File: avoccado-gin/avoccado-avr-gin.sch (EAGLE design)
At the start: 61 parts, among them Q1 16MHz, Q2 FET, U1 MPU-6000QFN-24, U2 MCP73831

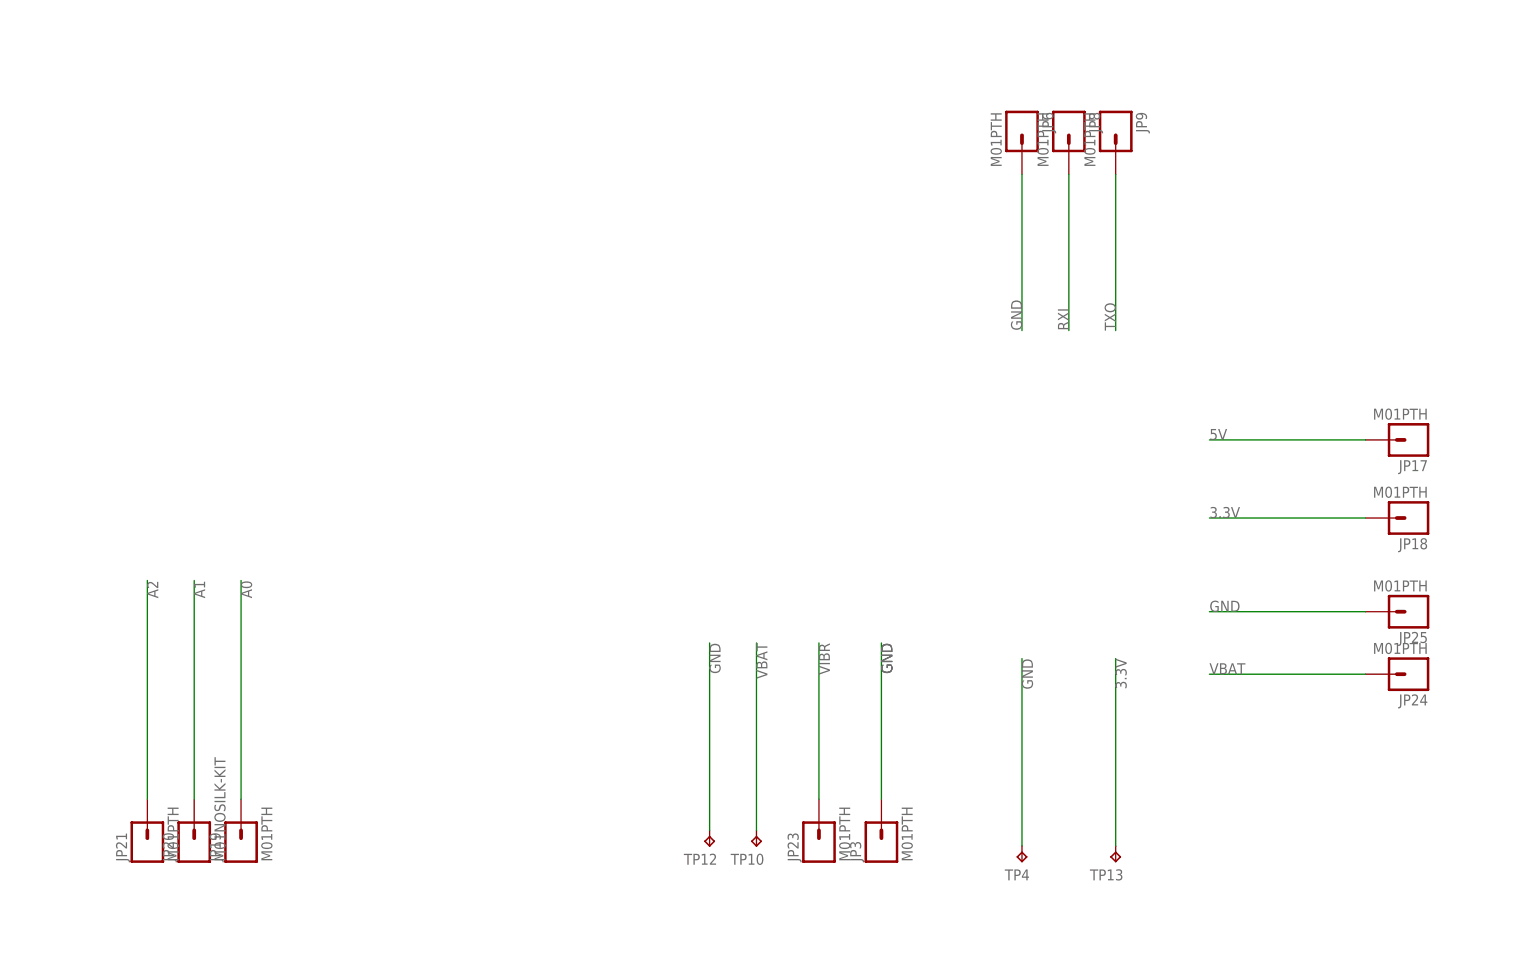
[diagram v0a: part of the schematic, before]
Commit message: cleanup unused headers
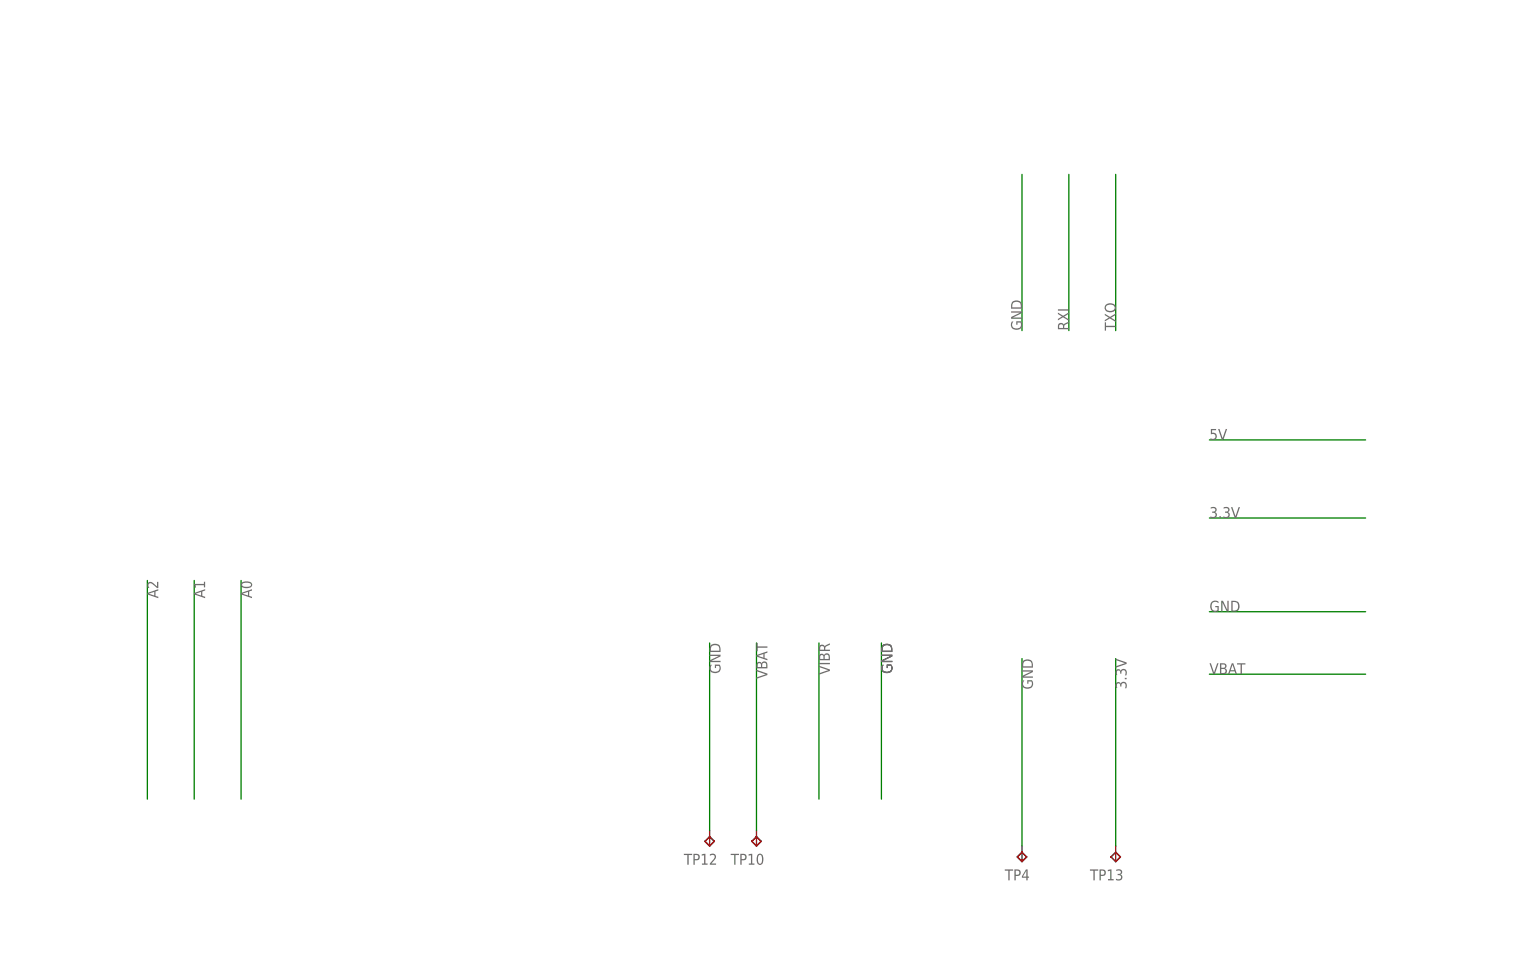
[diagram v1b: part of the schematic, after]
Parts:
- removed JP17, JP18, JP19, JP21, JP23, JP24, JP25, JP3, JP6, JP8, JP9: M01PTH, SparkFun-Connectors:M01PTH
- removed JP20: M01NOSILK-KIT, SparkFun-Connectors:M01NOSILK-KIT
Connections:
- net 3.3V: no longer JP18.1
- net 5V: no longer JP17.1
- net A0: no longer JP19.1
- net A1: no longer JP20.1
- net A2: no longer JP21.1
- net GND: no longer JP25.1, JP3.1, JP6.1
- net RXI: no longer JP8.1
- net TXO: no longer JP9.1
- net VBAT: no longer JP24.1
- net VIBR: no longer JP23.1
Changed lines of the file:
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@@
 <part name="R5" library="SparkFun-Resistors" deviceset="RESISTOR" device="0603" value="4.7M"/>
 <part name="R6" library="SparkFun-Resistors" deviceset="RESISTOR" device="0603" value="511R"/>
-<part name="JP6" library="SparkFun-Connectors" deviceset="M01" device="PTH" value="M01PTH"/>
-<part name="JP8" library="SparkFun-Connectors" deviceset="M01" device="PTH" value="M01PTH"/>
-<part name="JP9" library="SparkFun-Connectors" deviceset="M01" device="PTH" value="M01PTH"/>
-<part name="JP3" library="SparkFun-Connectors" deviceset="M01" device="PTH" value="M01PTH"/>
-<part name="JP17" library="SparkFun-Connectors" deviceset="M01" device="PTH" value="M01PTH"/>
-<part name="JP18" library="SparkFun-Connectors" deviceset="M01" device="PTH" value="M01PTH"/>
-<part name="JP19" library="SparkFun-Connectors" deviceset="M01" device="PTH" value="M01PTH"/>
-<part name="JP20" library="SparkFun-Connectors" deviceset="M01" device="NOSILK-KIT" value="M01NOSILK-KIT"/>
-<part name="JP21" library="SparkFun-Connectors" deviceset="M01" device="PTH" value="M01PTH"/>
 <part name="C5" library="SparkFun-Capacitors" deviceset="4.7UF-6.3V-10%(0603)" device="0603" value="4.7uF"/>
 <part name="C6" library="SparkFun-Capacitors" deviceset="4.7UF-6.3V-10%(0603)" device="0603" value="4.7uF"/>
-<part name="JP24" library="SparkFun-Connectors" deviceset="M01" device="PTH" value="M01PTH"/>
-<part name="JP23" library="SparkFun-Connectors" deviceset="M01" device="PTH" value="M01PTH"/>
-<part name="JP25" library="SparkFun-Connectors" deviceset="M01" device="PTH" value="M01PTH"/>
 <part name="JP2" library="SparkFun-Connectors" deviceset="M02" device="1X02_NO_SILK"/>
 <part name="JP27" library="SparkFun-Connectors" deviceset="M02" device="1X02_NO_SILK"/>
@@
 <instance part="R5" gate="G$1" x="45.72" y="76.2" rot="R90"/>
 <instance part="R6" gate="G$1" x="203.2" y="337.82" rot="R90"/>
-<instance part="JP6" gate="G$1" x="464.82" y="175.26" rot="R270"/>
-<instance part="JP8" gate="G$1" x="472.44" y="175.26" rot="R270"/>
-<instance part="JP9" gate="G$1" x="480.06" y="175.26" rot="R270"/>
-<instance part="JP3" gate="G$1" x="441.96" y="58.42" rot="R90"/>
-<instance part="JP17" gate="G$1" x="528.32" y="124.46" rot="R180"/>
-<instance part="JP18" gate="G$1" x="528.32" y="111.76" rot="R180"/>
-<instance part="JP19" gate="G$1" x="337.82" y="58.42" rot="R90"/>
-<instance part="JP20" gate="G$1" x="330.2" y="58.42" rot="R90"/>
-<instance part="JP21" gate="G$1" x="322.58" y="58.42" rot="R90"/>
 <instance part="C5" gate="G$1" x="40.64" y="264.16"/>
 <instance part="C6" gate="G$1" x="76.2" y="264.16"/>
-<instance part="JP24" gate="G$1" x="528.32" y="86.36" rot="R180"/>
-<instance part="JP23" gate="G$1" x="431.8" y="58.42" rot="R90"/>
-<instance part="JP25" gate="G$1" x="528.32" y="96.52" rot="R180"/>
 <instance part="JP2" gate="G$1" x="622.3" y="104.14"/>
 <instance part="JP27" gate="G$1" x="622.3" y="114.3"/>
@@
 <segment>
 <wire x1="464.82" y1="167.64" x2="464.82" y2="142.24" width="0.1524" layer="91"/>
-<pinref part="JP6" gate="G$1" pin="1"/>
 <label x="464.82" y="142.24" size="1.778" layer="95" rot="R90"/>
 <label x="441.96" y="91.44" size="1.778" layer="95" rot="R270"/>
@@
 <segment>
 <wire x1="441.96" y1="66.04" x2="441.96" y2="91.44" width="0.1524" layer="91"/>
-<pinref part="JP3" gate="G$1" pin="1"/>
 <label x="441.96" y="91.44" size="1.778" layer="95" rot="R270"/>
 </segment>
 <segment>
 <wire x1="520.7" y1="96.52" x2="495.3" y2="96.52" width="0.1524" layer="91"/>
-<pinref part="JP25" gate="G$1" pin="1"/>
 <label x="495.3" y="96.52" size="1.778" layer="95"/>
 </segment>
@@
 <segment>
 <wire x1="480.06" y1="142.24" x2="480.06" y2="167.64" width="0.1524" layer="91"/>
-<pinref part="JP9" gate="G$1" pin="1"/>
 <label x="480.06" y="142.24" size="1.778" layer="95" rot="R90"/>
 </segment>
@@
 <segment>
 <wire x1="495.3" y1="111.76" x2="520.7" y2="111.76" width="0.1524" layer="91"/>
-<pinref part="JP18" gate="G$1" pin="1"/>
 <label x="495.3" y="111.76" size="1.778" layer="95"/>
 </segment>
@@
 <segment>
 <wire x1="322.58" y1="101.6" x2="322.58" y2="66.04" width="0.1524" layer="91"/>
-<pinref part="JP21" gate="G$1" pin="1"/>
 <label x="322.58" y="101.6" size="1.778" layer="95" rot="R270"/>
 </segment>
@@
 <segment>
 <wire x1="330.2" y1="101.6" x2="330.2" y2="66.04" width="0.1524" layer="91"/>
-<pinref part="JP20" gate="G$1" pin="1"/>
 <label x="330.2" y="101.6" size="1.778" layer="95" rot="R270"/>
 </segment>
@@
 <segment>
 <wire x1="337.82" y1="101.6" x2="337.82" y2="66.04" width="0.1524" layer="91"/>
-<pinref part="JP19" gate="G$1" pin="1"/>
 <label x="337.82" y="101.6" size="1.778" layer="95" rot="R270"/>
 </segment>
@@
 <segment>
 <wire x1="472.44" y1="142.24" x2="472.44" y2="167.64" width="0.1524" layer="91"/>
-<pinref part="JP8" gate="G$1" pin="1"/>
 <label x="472.44" y="142.24" size="1.778" layer="95" rot="R90"/>
 </segment>
@@
 <segment>
 <wire x1="495.3" y1="124.46" x2="520.7" y2="124.46" width="0.1524" layer="91"/>
-<pinref part="JP17" gate="G$1" pin="1"/>
 <label x="495.3" y="124.46" size="1.778" layer="95"/>
 </segment>
@@
 </segment>
 <segment>
-<pinref part="JP23" gate="G$1" pin="1"/>
 <label x="431.8" y="91.44" size="1.778" layer="95" rot="R270"/>
 <wire x1="431.8" y1="66.04" x2="431.8" y2="91.44" width="0.2032" layer="91"/>
@@
 <segment>
 <wire x1="520.7" y1="86.36" x2="495.3" y2="86.36" width="0.1524" layer="91"/>
-<pinref part="JP24" gate="G$1" pin="1"/>
 <label x="495.3" y="86.36" size="1.778" layer="95"/>
 </segment>

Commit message: add RX and TX test points
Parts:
- added TP1, TP2, TP6, TP7, TP8: TPTP20R, testpad:TPTP20R
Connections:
- net A1: now also TP8.TP
- net A7-NRF-IRQ: no longer JP29.2
- net RESET: now also TP7.TP
- net RXI: now also TP2.TP
- net TXO: now also TP6.TP
- net VIBR: now also TP1.TP
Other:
- note added: "NRF24L01+ board header SPI (IRQ NC)"
- note removed: "NRF24L01+ board header SPI (IRQ at ADC7 / A7)"
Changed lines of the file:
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@@
 <part name="GND17" library="SparkFun" deviceset="GND" device=""/>
 <part name="P+5" library="SparkFun" deviceset="3.3V" device="" value="VCC"/>
+<part name="TP1" library="testpad" deviceset="TP" device="TP20R"/>
+<part name="TP2" library="testpad" deviceset="TP" device="TP20R"/>
+<part name="TP6" library="testpad" deviceset="TP" device="TP20R"/>
+<part name="TP7" library="testpad" deviceset="TP" device="TP20R"/>
+<part name="TP8" library="testpad" deviceset="TP" device="TP20R"/>
 </parts>
 <sheets>
 <sheet>
 <plain>
-<text x="650.24" y="96.52" size="1.778" layer="91" rot="R180">NRF24L01+ board header SPI (IRQ at ADC7 / A7)</text>
+<text x="650.24" y="96.52" size="1.778" layer="91" rot="R180">NRF24L01+ board header SPI (IRQ NC)</text>
 <text x="175.26" y="162.56" size="1.778" layer="91">AtMega 328p</text>
 <text x="193.04" y="386.08" size="1.778" layer="91">LiPo 1c charge IC</text>
@@
 <attribute name="VALUE" x="334.264" y="336.296" size="1.778" layer="96"/>
 </instance>
+<instance part="TP1" gate="G$1" x="431.8" y="63.5" rot="R180"/>
+<instance part="TP2" gate="G$1" x="472.44" y="170.18"/>
+<instance part="TP6" gate="G$1" x="480.06" y="170.18"/>
+<instance part="TP7" gate="G$1" x="457.2" y="170.18"/>
+<instance part="TP8" gate="G$1" x="330.2" y="63.5" rot="R180"/>
 </instances>
 <busses>
@@
 <pinref part="U3" gate="U$1" pin="PC6(/RESET)"/>
 </segment>
+<segment>
+<wire x1="457.2" y1="167.64" x2="457.2" y2="142.24" width="0.1524" layer="91"/>
+<label x="457.2" y="142.24" size="1.778" layer="95" rot="R90"/>
+<pinref part="TP7" gate="G$1" pin="TP"/>
+</segment>
 </net>
 <net name="SCK" class="0">
@@
 <wire x1="480.06" y1="142.24" x2="480.06" y2="167.64" width="0.1524" layer="91"/>
 <label x="480.06" y="142.24" size="1.778" layer="95" rot="R90"/>
+<pinref part="TP6" gate="G$1" pin="TP"/>
 </segment>
 </net>
@@
 <wire x1="330.2" y1="101.6" x2="330.2" y2="66.04" width="0.1524" layer="91"/>
 <label x="330.2" y="101.6" size="1.778" layer="95" rot="R270"/>
+<pinref part="TP8" gate="G$1" pin="TP"/>
 </segment>
 </net>
@@
 <wire x1="472.44" y1="142.24" x2="472.44" y2="167.64" width="0.1524" layer="91"/>
 <label x="472.44" y="142.24" size="1.778" layer="95" rot="R90"/>
+<pinref part="TP2" gate="G$1" pin="TP"/>
 </segment>
 </net>
@@
 <label x="431.8" y="91.44" size="1.778" layer="95" rot="R270"/>
 <wire x1="431.8" y1="66.04" x2="431.8" y2="91.44" width="0.2032" layer="91"/>
+<pinref part="TP1" gate="G$1" pin="TP"/>
 </segment>
 </net>
@@
 <pinref part="U3" gate="U$1" pin="ADC7"/>
 </segment>
-<segment>
-<wire x1="647.7" y1="137.16" x2="629.92" y2="137.16" width="0.1524" layer="91"/>
-<pinref part="JP29" gate="G$1" pin="2"/>
-<label x="647.7" y="137.16" size="1.778" layer="95" rot="R180"/>
-</segment>
-</net>
+</net>

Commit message: no airwires left :shipit:
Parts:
- added TP9: TPTP20R, testpad:TPTP20R
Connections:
- net 3.3V: now also TP9.TP
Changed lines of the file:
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@@
 <part name="TP7" library="testpad" deviceset="TP" device="TP20R"/>
 <part name="TP8" library="testpad" deviceset="TP" device="TP20R"/>
+<part name="TP9" library="testpad" deviceset="TP" device="TP20R"/>
 </parts>
 <sheets>
@@
 <instance part="TP7" gate="G$1" x="457.2" y="170.18"/>
 <instance part="TP8" gate="G$1" x="330.2" y="63.5" rot="R180"/>
+<instance part="TP9" gate="G$1" x="401.32" y="58.42" rot="R180"/>
 </instances>
 <busses>
@@
 <pinref part="P+5" gate="G$1" pin="3.3V"/>
 </segment>
-</net>
+<segment>
+<wire x1="401.32" y1="91.44" x2="401.32" y2="60.96" width="0.1524" layer="91"/>
+<pinref part="TP9" gate="G$1" pin="TP"/>
+<label x="401.32" y="91.44" size="1.778" layer="95" rot="R270"/>
+</segment>
+</net>
